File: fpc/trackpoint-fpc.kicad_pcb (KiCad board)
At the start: 2 copper layers, 10.2 x 22.1 mm, 3 parts, among them P1 CONN_8, P2 CONN_5, P3 CONN_8

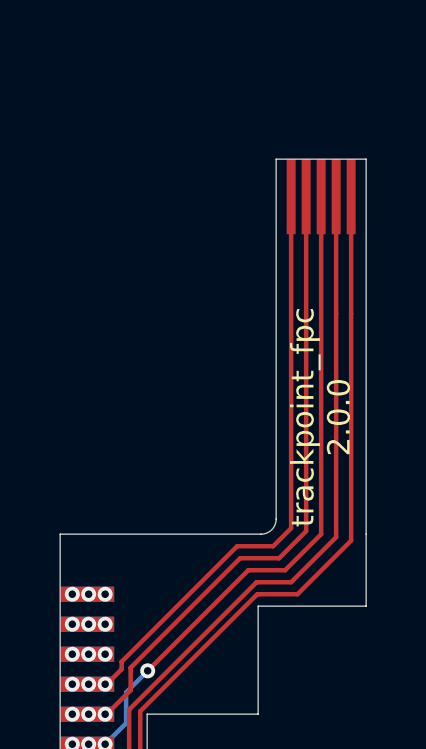
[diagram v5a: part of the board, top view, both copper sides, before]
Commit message: Update FPC based on CAD.
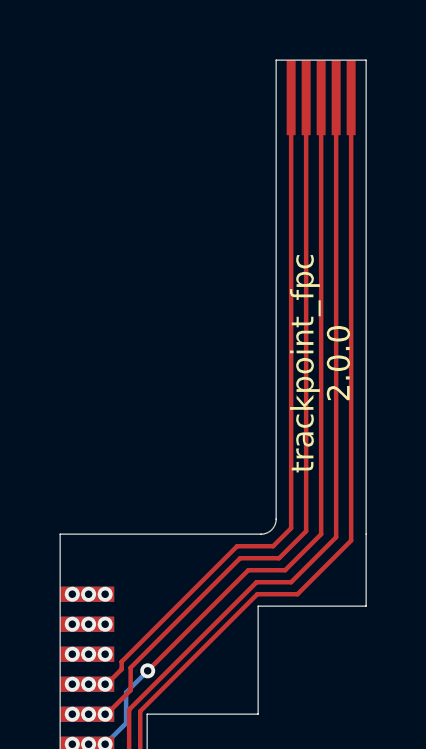
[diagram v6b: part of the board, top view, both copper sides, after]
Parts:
- moved P2 3.30 mm to (198.3, 125.2)
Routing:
- net /VCC: track 23.4 -> 28.0 mm
- net /GND: track 22.1 -> 26.6 mm
- net /RESET: track 21.1 -> 25.3 mm
- net /DATA: track 18.7 -> 22.8 mm
- net /CLK: track 19.9 -> 23.9 mm
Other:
- board size 10.2 x 22.1 mm -> 10.2 x 25.4 mm
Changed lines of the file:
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@@
     (thickness 1.6)
     (drawings 30)
-    (tracks 61)
+    (tracks 59)
     (zones 0)
     (modules 3)
@@
   )
   (module UGL:Trackpoint_FPC_5x0.5_pads (layer F.Cu)
-    (at 198.3 128.45)
+    (at 198.3 125.15)
     (attr smd)
     (fp_text reference P2 (at 0 3.65) (layer F.SilkS) hide
@@
       (effects (font (size 1 1) (thickness 0.15)))
     )
+    (pad 1 smd rect (at -1 0) (size 0.3 2.5) (layers F.Cu F.Paste F.Mask)
+      (net 5 /DATA))
+    (pad 2 smd rect (at -0.5 0) (size 0.3 2.5) (layers F.Cu F.Paste F.Mask)
+      (net 4 /CLK))
+    (pad 3 smd rect (at 0 0) (size 0.3 2.5) (layers F.Cu F.Paste F.Mask)
+      (net 3 /RESET))
+    (pad 4 smd rect (at 0.5 0) (size 0.3 2.5) (layers F.Cu F.Paste F.Mask)
+      (net 2 /GND))
     (pad 5 smd rect (at 1 0) (size 0.3 2.5) (layers F.Cu F.Paste F.Mask)
       (net 1 /VCC))
-    (pad 4 smd rect (at 0.5 0) (size 0.3 2.5) (layers F.Cu F.Paste F.Mask)
-      (net 2 /GND))
-    (pad 3 smd rect (at 0 0) (size 0.3 2.5) (layers F.Cu F.Paste F.Mask)
-      (net 3 /RESET))
-    (pad 2 smd rect (at -0.5 0) (size 0.3 2.5) (layers F.Cu F.Paste F.Mask)
-      (net 4 /CLK))
-    (pad 1 smd rect (at -1 0) (size 0.3 2.5) (layers F.Cu F.Paste F.Mask)
-      (net 5 /DATA))
   )
   (module UGL:Trackpoint_FPC_8x1_pads locked (layer F.Cu)
@@
       (net 1 /VCC))
   )
-  (gr_line (start 199.8 132.2) (end 196.8 132.2) (layer Cmts.User) (width 0.05))
-  (gr_text "trackpoint_fpc\n2.0.0" (at 198.3 135.8 90) (layer F.SilkS)
+  (gr_line (start 199.8 128.9) (end 196.8 128.9) (layer Cmts.User) (width 0.05))
+  (gr_text "trackpoint_fpc\n2.0.0" (at 198.3 134 90) (layer F.SilkS)
     (effects (font (size 0.75 0.75) (thickness 0.15)))
   )
-  (gr_text "Stiffener BOTTOM" (at 206.6 129.7) (layer Dwgs.User)
+  (gr_text "Stiffener BOTTOM" (at 206.6 126.4) (layer Dwgs.User)
     (effects (font (size 1 1) (thickness 0.15)))
   )
-  (gr_text "5.00 mm" (at 205.35 122.1 90) (layer Dwgs.User)
+  (gr_text "5.00 mm" (at 205.35 118.8 90) (layer Dwgs.User)
     (effects (font (size 1 1) (thickness 0.15)))
   )
-  (gr_line (start 206.25 126.4) (end 206.35 126.4) (layer Dwgs.User) (width 0.15))
-  (gr_line (start 206.15 126.3) (end 206.45 126.3) (layer Dwgs.User) (width 0.15))
-  (gr_line (start 206.2 132.9) (end 206.4 132.9) (layer Dwgs.User) (width 0.15))
-  (gr_line (start 206.15 133) (end 206.4 133) (layer Dwgs.User) (width 0.15))
-  (gr_line (start 206.5 133.1) (end 206.1 133.1) (layer Dwgs.User) (width 0.15))
-  (gr_line (start 206.3 132.2) (end 206.5 133.1) (layer Dwgs.User) (width 0.15))
-  (gr_line (start 206.3 132.2) (end 206.1 133.1) (layer Dwgs.User) (width 0.15))
-  (gr_line (start 206.3 132.2) (end 206.3 134.75) (layer Dwgs.User) (width 0.15))
-  (gr_line (start 206.5 126.15) (end 206.1 126.15) (layer Dwgs.User) (width 0.15))
-  (gr_line (start 206.3 127.2) (end 206.5 126.15) (layer Dwgs.User) (width 0.15))
-  (gr_line (start 206.3 127.2) (end 206.1 126.15) (layer Dwgs.User) (width 0.15))
-  (gr_line (start 206.3 127.2) (end 206.3 118.5) (layer Dwgs.User) (width 0.15))
-  (gr_line (start 199.8 132.2) (end 207.3 132.2) (layer Dwgs.User) (width 0.15))
-  (gr_line (start 199.8 127.2) (end 207.3 127.2) (layer Dwgs.User) (width 0.15))
-  (gr_line (start 199.8 127.1975) (end 199.8 139.6975) (angle 90) (layer Edge.Cuts) (width 0.01))
-  (gr_line (start 196.8 127.1975) (end 196.8 139.1975) (angle 90) (layer Edge.Cuts) (width 0.01))
+  (gr_line (start 206.25 123.1) (end 206.35 123.1) (layer Dwgs.User) (width 0.15))
+  (gr_line (start 206.15 123) (end 206.45 123) (layer Dwgs.User) (width 0.15))
+  (gr_line (start 206.2 129.6) (end 206.4 129.6) (layer Dwgs.User) (width 0.15))
+  (gr_line (start 206.15 129.7) (end 206.4 129.7) (layer Dwgs.User) (width 0.15))
+  (gr_line (start 206.5 129.8) (end 206.1 129.8) (layer Dwgs.User) (width 0.15))
+  (gr_line (start 206.3 128.9) (end 206.5 129.8) (layer Dwgs.User) (width 0.15))
+  (gr_line (start 206.3 128.9) (end 206.1 129.8) (layer Dwgs.User) (width 0.15))
+  (gr_line (start 206.3 128.9) (end 206.3 131.45) (layer Dwgs.User) (width 0.15))
+  (gr_line (start 206.5 122.85) (end 206.1 122.85) (layer Dwgs.User) (width 0.15))
+  (gr_line (start 206.3 123.9) (end 206.5 122.85) (layer Dwgs.User) (width 0.15))
+  (gr_line (start 206.3 123.9) (end 206.1 122.85) (layer Dwgs.User) (width 0.15))
+  (gr_line (start 206.3 123.9) (end 206.3 115.2) (layer Dwgs.User) (width 0.15))
+  (gr_line (start 199.8 128.9) (end 207.3 128.9) (layer Dwgs.User) (width 0.15))
+  (gr_line (start 199.8 123.9) (end 207.3 123.9) (layer Dwgs.User) (width 0.15))
+  (gr_line (start 199.8 123.8975) (end 199.8 139.6975) (angle 90) (layer Edge.Cuts) (width 0.01))
+  (gr_line (start 196.8 123.8975) (end 196.8 139.1975) (angle 90) (layer Edge.Cuts) (width 0.01))
   (gr_line (start 196.3 139.6975) (end 189.6 139.6975) (angle 90) (layer Edge.Cuts) (width 0.01))
   (gr_line (start 192.5 149.2975) (end 192.5 145.6975) (angle 90) (layer Edge.Cuts) (width 0.01))
@@
   (gr_line (start 199.8 142.0975) (end 199.8 139.6975) (angle 90) (layer Edge.Cuts) (width 0.01))
   (gr_line (start 196.2 142.0975) (end 199.8 142.0975) (angle 90) (layer Edge.Cuts) (width 0.01))
-  (gr_line (start 199.8 127.1975) (end 196.8 127.1975) (angle 90) (layer Edge.Cuts) (width 0.01))
+  (gr_line (start 199.8 123.8975) (end 196.8 123.8975) (angle 90) (layer Edge.Cuts) (width 0.01))
   (gr_arc (start 196.300006 139.197511) (end 196.3 139.6975) (angle -90.00254177) (layer Edge.Cuts) (width 0.01))
-  (segment (start 199.3 139.912139) (end 199.3 132.35) (width 0.15) (layer F.Cu) (net 1))
   (segment (start 197.512139 141.7) (end 199.3 139.912139) (width 0.15) (layer F.Cu) (net 1))
   (segment (start 192.26999 145.602227) (end 196.172217 141.7) (width 0.15) (layer F.Cu) (net 1))
@@
   (segment (start 196.172217 141.7) (end 197.512139 141.7) (width 0.15) (layer F.Cu) (net 1))
   (segment (start 191.55 148.7) (end 192.26999 147.98001) (width 0.15) (layer F.Cu) (net 1))
-  (segment (start 199.3 132.35) (end 199.3 129.7) (width 0.15) (layer F.Cu) (net 1))
   (via (at 190.005 148.7) (size 0.5) (drill 0.25) (layers F.Cu B.Cu) (net 1))
   (via (at 191.1 148.7) (size 0.5) (drill 0.25) (layers F.Cu B.Cu) (net 1))
   (via (at 190.55 148.7) (size 0.5) (drill 0.25) (layers F.Cu B.Cu) (net 1))
   (segment (start 191.55 148.7) (end 191.1 148.7) (width 0.15) (layer F.Cu) (net 1))
-  (segment (start 198.8 132.35) (end 198.8 129.7) (width 0.15) (layer F.Cu) (net 2))
+  (segment (start 199.3 139.912139) (end 199.3 125.15) (width 0.15) (layer F.Cu) (net 1))
   (segment (start 197.3 141.3) (end 198.8 139.8) (width 0.15) (layer F.Cu) (net 2))
-  (segment (start 198.8 139.8) (end 198.8 132.35) (width 0.15) (layer F.Cu) (net 2))
   (segment (start 191.899991 145.547947) (end 196.147938 141.3) (width 0.15) (layer F.Cu) (net 2))
   (segment (start 191.55 147.7) (end 191.899991 147.350009) (width 0.15) (layer F.Cu) (net 2))
@@
   (via (at 191.1 147.7) (size 0.5) (drill 0.25) (layers F.Cu B.Cu) (net 2))
   (segment (start 191.55 147.7) (end 191.1 147.7) (width 0.15) (layer F.Cu) (net 2))
+  (segment (start 198.8 139.8) (end 198.8 125.25) (width 0.15) (layer F.Cu) (net 2))
   (via (at 190.005 146.7) (size 0.5) (drill 0.25) (layers F.Cu B.Cu) (net 3))
   (via (at 190.55 146.7) (size 0.5) (drill 0.25) (layers F.Cu B.Cu) (net 3))
@@
   (segment (start 191.8 146) (end 191.8 144.971767) (width 0.15) (layer B.Cu) (net 3))
   (segment (start 191.1 146.7) (end 191.8 146) (width 0.15) (layer B.Cu) (net 3))
-  (segment (start 198.3 139.7) (end 198.3 129.4) (width 0.15) (layer F.Cu) (net 3))
+  (segment (start 198.3 139.7) (end 198.3 125.2) (width 0.15) (layer F.Cu) (net 3))
   (segment (start 196.9 140.5) (end 197.8 139.6) (width 0.15) (layer F.Cu) (net 4))
   (segment (start 195.6 140.5) (end 196.9 140.5) (width 0.15) (layer F.Cu) (net 4))
@@
   (via (at 190.55 145.7) (size 0.5) (drill 0.25) (layers F.Cu B.Cu) (net 4))
   (via (at 191.1 145.7) (size 0.5) (drill 0.25) (layers F.Cu B.Cu) (net 4))
-  (segment (start 197.8 139.6) (end 197.8 129.3) (width 0.15) (layer F.Cu) (net 4))
+  (segment (start 197.8 139.6) (end 197.8 125.3) (width 0.15) (layer F.Cu) (net 4))
   (segment (start 195.5 140.1) (end 196.7 140.1) (width 0.15) (layer F.Cu) (net 5))
   (segment (start 191.65 143.95) (end 195.5 140.1) (width 0.15) (layer F.Cu) (net 5))
@@
   (via (at 190.55 144.7) (size 0.5) (drill 0.25) (layers F.Cu B.Cu) (net 5))
   (via (at 191.1 144.7) (size 0.5) (drill 0.25) (layers F.Cu B.Cu) (net 5))
-  (segment (start 197.3 139.5) (end 197.3 129.3) (width 0.15) (layer F.Cu) (net 5))
+  (segment (start 197.3 139.5) (end 197.3 125.15) (width 0.15) (layer F.Cu) (net 5))
   (via (at 190.005 143.7) (size 0.5) (drill 0.25) (layers F.Cu B.Cu) (net 6))
   (via (at 190.55 143.7) (size 0.5) (drill 0.25) (layers F.Cu B.Cu) (net 6))

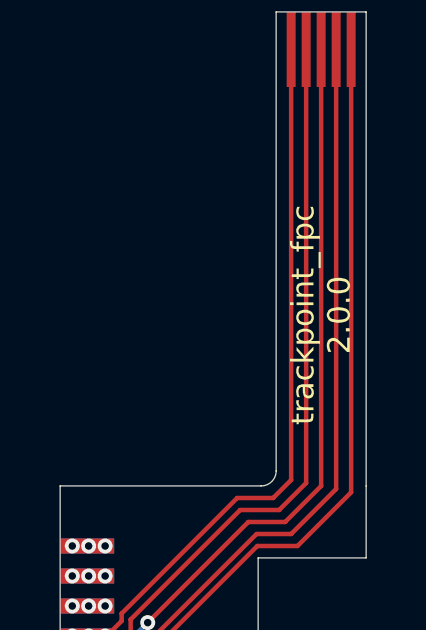
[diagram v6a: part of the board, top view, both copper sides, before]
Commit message: Bump FPC version to 2.1.0
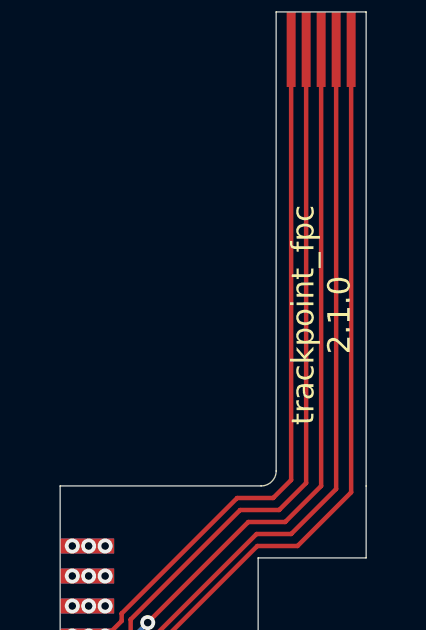
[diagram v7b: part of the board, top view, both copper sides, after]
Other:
- board text added: "trackpoint_fpc 2.1.0"
- board text removed: "trackpoint_fpc 2.0.0"
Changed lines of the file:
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@@
   (title_block
     (title "UHK Trackpoint FPC")
-    (rev 2.0.0)
+    (rev 2.1.0)
     (company "Ultimate Gadget Laboratories Kft.")
   )
@@
   )
   (gr_line (start 199.8 128.9) (end 196.8 128.9) (layer Cmts.User) (width 0.05))
-  (gr_text "trackpoint_fpc\n2.0.0" (at 198.3 134 90) (layer F.SilkS)
+  (gr_text "trackpoint_fpc\n2.1.0" (at 198.3 134 90) (layer F.SilkS)
     (effects (font (size 0.75 0.75) (thickness 0.15)))
   )
